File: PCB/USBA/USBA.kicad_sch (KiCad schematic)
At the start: 24 parts, among them J1 USB_A, J2 Shelly, J3 USB-PROG, U2 ESP32-S3-MINI-1, U5 MD8942, U7 SHT40

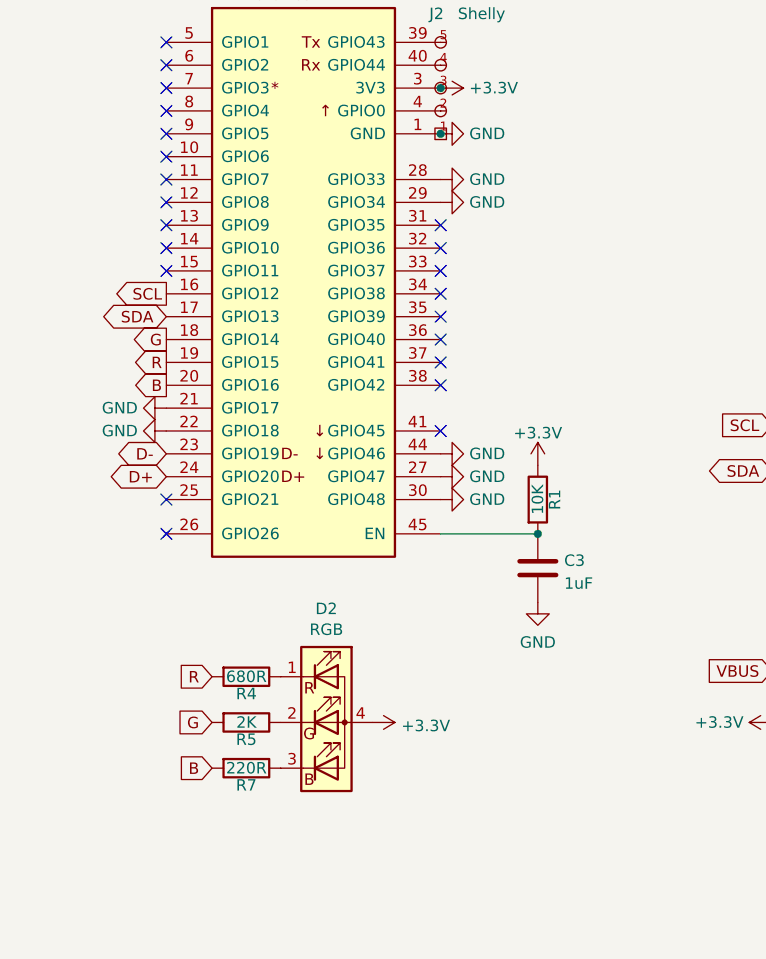
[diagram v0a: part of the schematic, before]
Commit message: Changed to WS2812
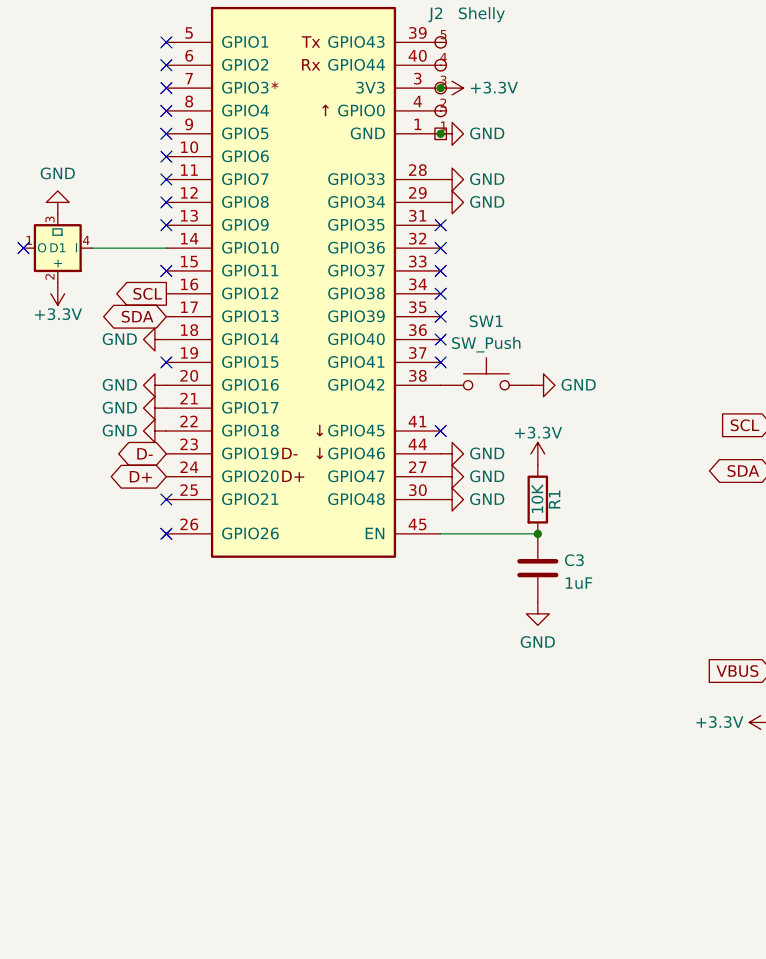
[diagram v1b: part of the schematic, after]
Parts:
- removed D2: RGB, RevK:LED-RGB-1.6x1.6, symbol Device:LED_RGBA
- removed R4: 680R, RevK:R_0402, symbol Device:R
- removed R5: 2K, RevK:R_0402, symbol Device:R
- removed R7: 220R, RevK:R_0402, symbol Device:R
- added D1: XL-1010RGBC-WS2812B, RevK:SMD1010, symbol RevK:WS2812B-1mm
- added SW1: SW_Push, RevK:TS-1092S-B3D2-G, symbol Switch:SW_Push
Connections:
- net B is gone; now on net GND: U2.20 (GPIO16)
- net G is gone; now on net GND: U2.18 (GPIO14)
- net +3.3V: now also D1.2 (+)
- net GND: now also D1.3 (⏚), SW1.2
- net at U2.14 (GPIO10): now also D1.4 (I)
- net at U2.38 (GPIO42): now also SW1.1
- net R: no longer names the net of U2.19 (GPIO15)

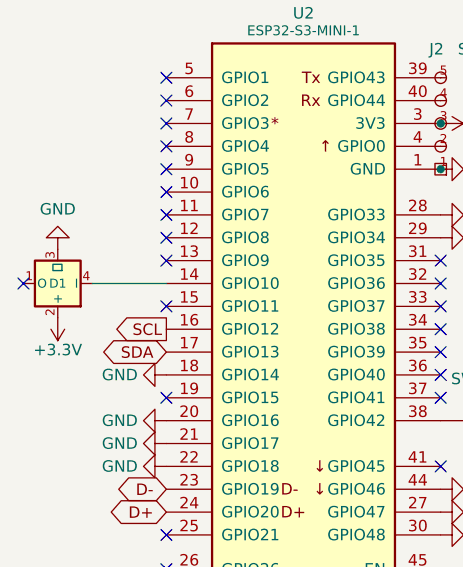
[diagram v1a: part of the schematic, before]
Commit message: Slight angle fixed
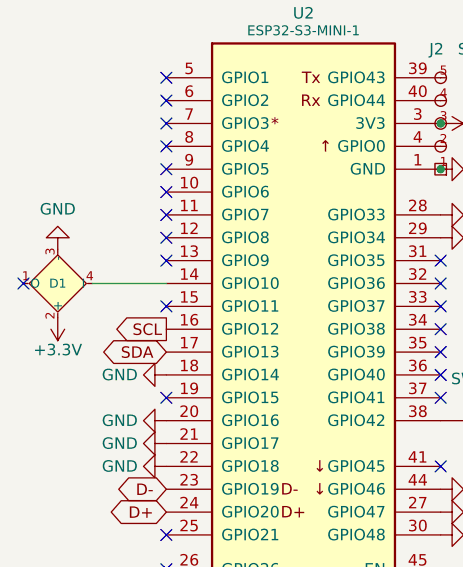
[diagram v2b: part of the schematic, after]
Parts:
- V1, V2: footprint RevK:VCUT70 -> RevK:VCUT70N
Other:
- moved on the sheet: D1
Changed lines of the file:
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@@
     )
   )
-  (symbol (lib_id "RevK:WS2812B-1mm") (at 81.915 75.565 180) (unit 1)
-    (in_bom yes) (on_board yes) (dnp no) (fields_autoplaced)
+  (symbol (lib_id "RevK:WS2812B-1mm") (at 81.915 75.565 0) (mirror y) (unit 1)
+    (in_bom yes) (on_board yes) (dnp no)
     (property "Reference" "D1" (at 81.915 75.565 0) (do_not_autoplace)
       (effects (font (size 1 1)))
     )
-    (property "Value" "XL-1010RGBC-WS2812B" (at 80.645 69.85 0)
+    (property "Value" "XL-1010RGBC-WS2812B" (at 80.645 81.28 0)
       (effects (font (size 1 1)) (justify left top) hide)
     )
-    (property "Footprint" "RevK:SMD1010" (at 80.645 67.945 0)
+    (property "Footprint" "RevK:SMD1010" (at 80.645 83.185 0)
       (effects (font (size 1 1)) (justify left top) hide)
     )
-    (property "Datasheet" "https://datasheet.lcsc.com/lcsc/2301111010_XINGLIGHT-XL-1010RGBC-WS2812B_C5349953.pdf" (at 80.645 66.04 0)
+    (property "Datasheet" "https://datasheet.lcsc.com/lcsc/2301111010_XINGLIGHT-XL-1010RGBC-WS2812B_C5349953.pdf" (at 80.645 85.09 0)
       (effects (font (size 1 1)) (justify left top) hide)
     )
-    (property "LCSC Part #" "C5349953" (at 80.645 64.135 0)
+    (property "LCSC Part #" "C5349953" (at 80.645 86.995 0)
       (effects (font (size 1 1)) (justify left top) hide)
     )
@@
       (effects (font (size 1.27 1.27)) hide)
     )
-    (property "Footprint" "RevK:VCUT70" (at 250.19 177.165 0)
+    (property "Footprint" "RevK:VCUT70N" (at 250.19 177.165 0)
       (effects (font (size 1.27 1.27)) hide)
     )
@@
       (effects (font (size 1.27 1.27)) hide)
     )
-    (property "Footprint" "RevK:VCUT70" (at 250.19 170.815 0)
+    (property "Footprint" "RevK:VCUT70N" (at 250.19 170.815 0)
       (effects (font (size 1.27 1.27)) hide)
     )

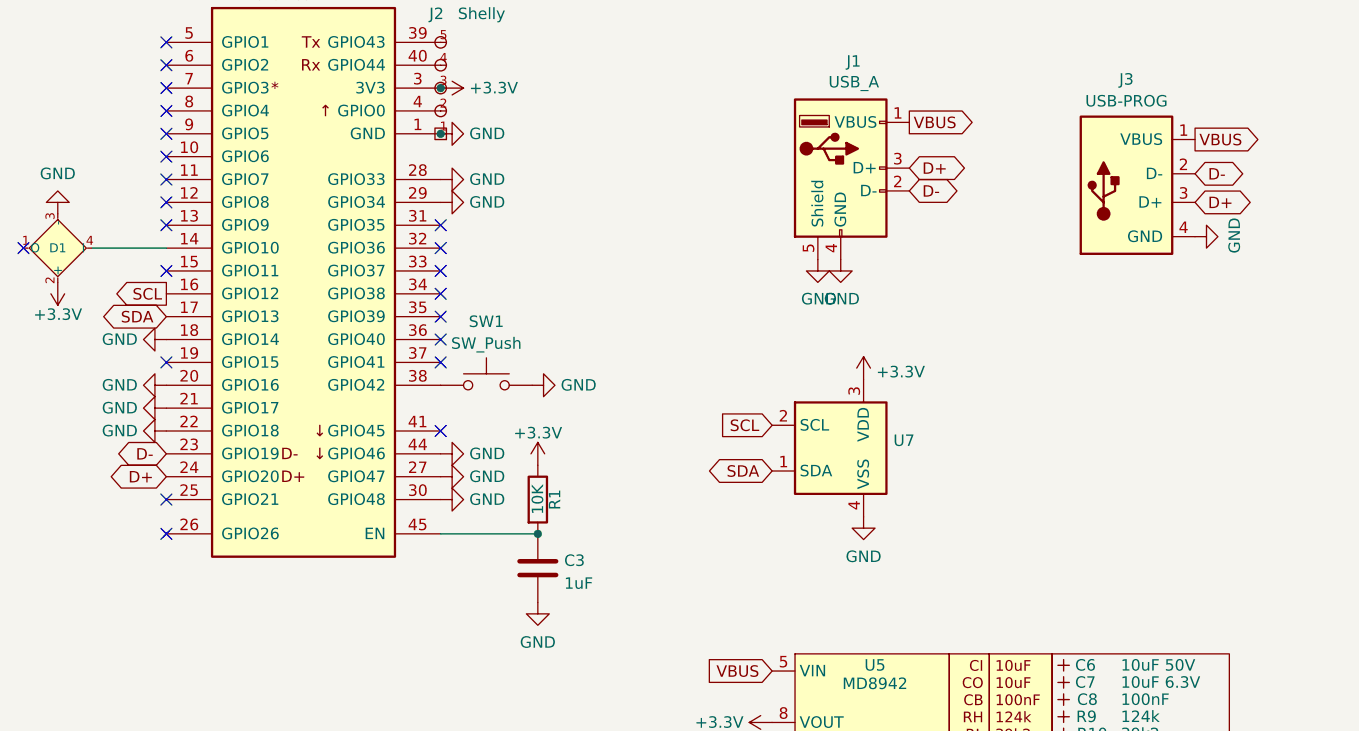
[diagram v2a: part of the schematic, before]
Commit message: Changed to light sensor
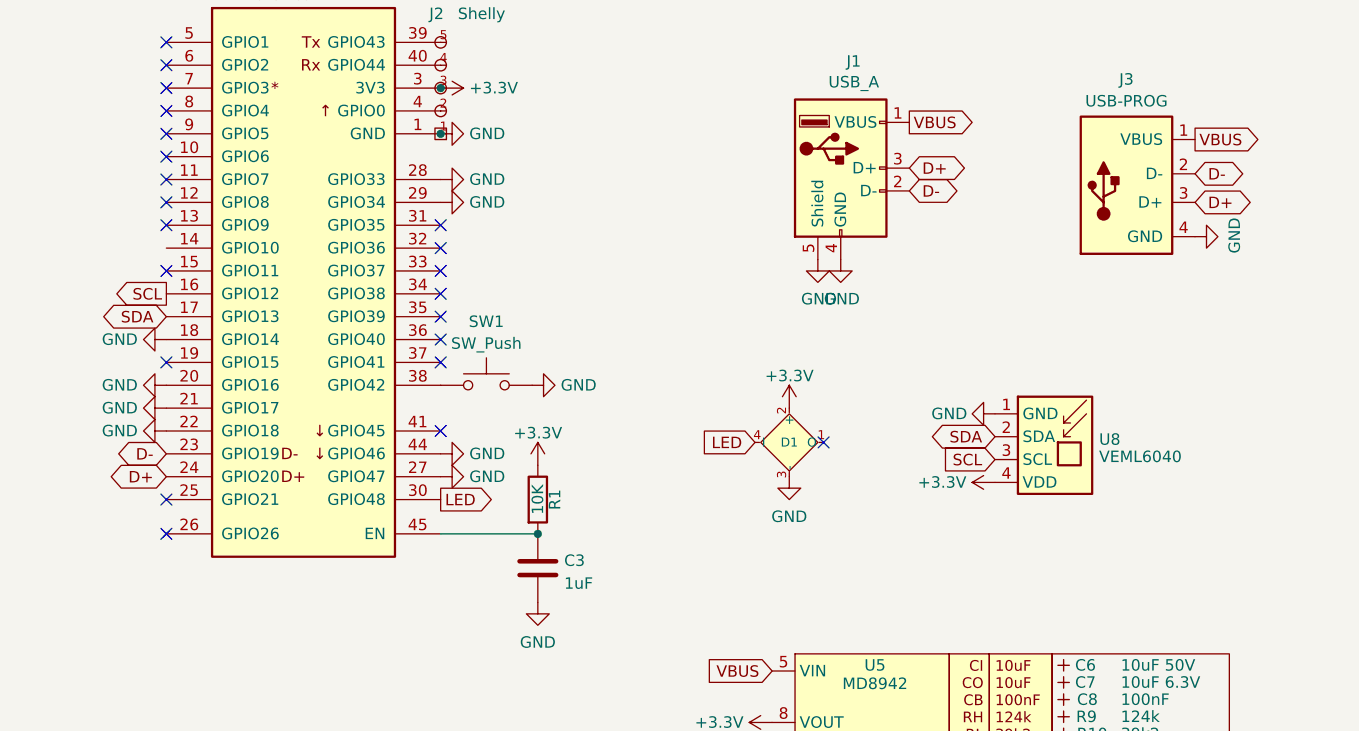
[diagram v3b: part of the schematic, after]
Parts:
- removed U7: SHT40, RevK:Sensirion_DFN-4_1.5x1.5mm_P0.5mm_SHT4x, symbol RevK:SHT40
- added U8: VEML6040, RevK:VEML6040, symbol RevK:VEML6040
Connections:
- net +3.3V: now also U8.4 (VDD)
- net GND: now also U8.1 (GND); no longer U2.30 (GPIO48)
- net SCL: now also U8.3 (SCL)
- net SDA: now also U8.2 (SDA)
- net at U2.14 (GPIO10): no longer D1.4 (I)
- new net LED: D1.4 (I), U2.30 (GPIO48)
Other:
- moved on the sheet: D1

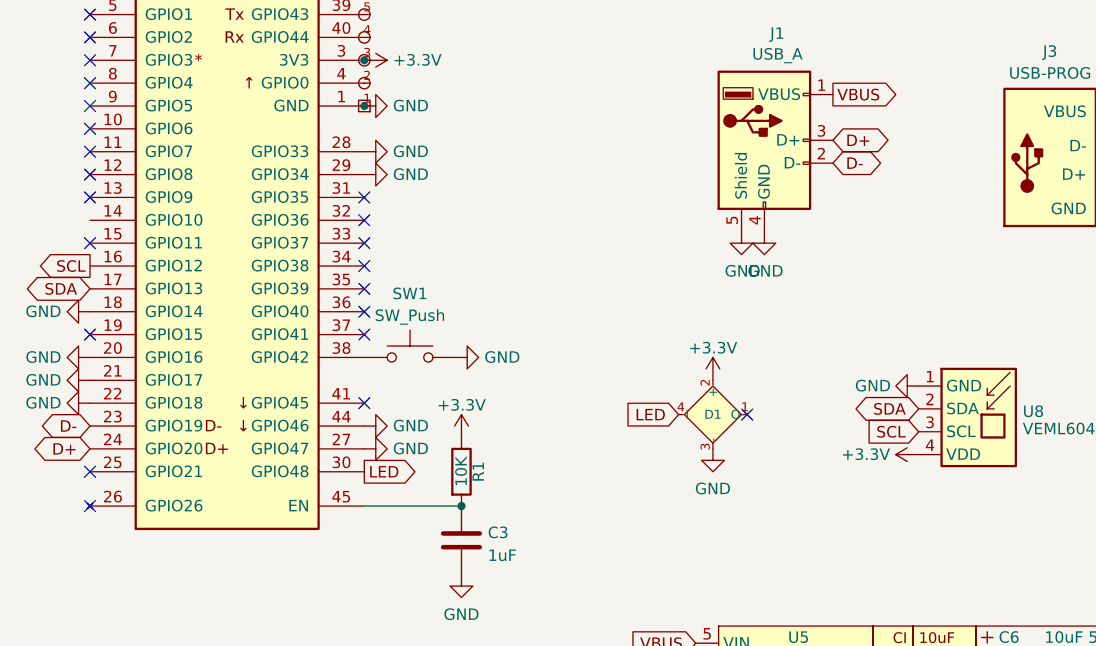
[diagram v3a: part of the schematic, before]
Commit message: Added 3 pads for LED
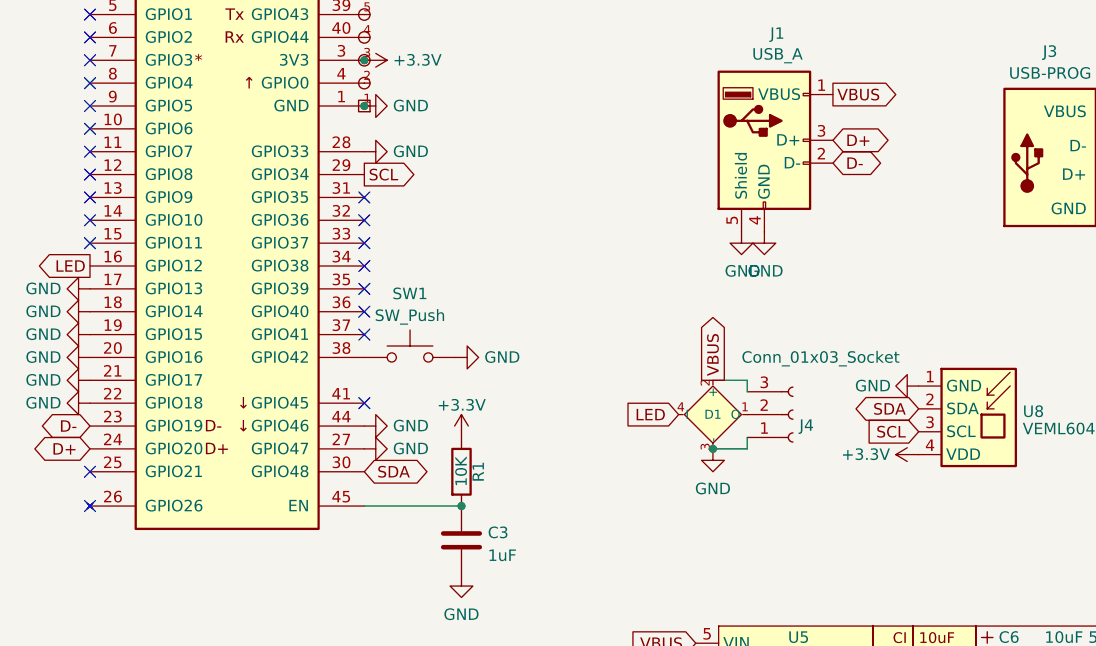
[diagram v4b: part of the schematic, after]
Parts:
- added J4: Conn_01x03_Socket, RevK:PinHeader_1x03_P2.54mm, symbol Connector:Conn_01x03_Socket
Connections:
- net +3.3V: no longer D1.2 (+)
- net GND: now also U2.17 (GPIO13), U2.19 (GPIO15), J4.1 (Pin_1); no longer U2.29 (GPIO34)
- net LED: now also U2.16 (GPIO12); no longer U2.30 (GPIO48)
- net SCL: now also U2.29 (GPIO34); no longer U2.16 (GPIO12)
- net SDA: now also U2.30 (GPIO48); no longer U2.17 (GPIO13)
- net VBUS: now also D1.2 (+), J4.3 (Pin_3)
- net at D1.1 (O): now also J4.2 (Pin_2)
- no-connect marks 23 -> 22
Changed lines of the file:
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@@
   (junction (at 124.46 62.865) (diameter 0) (color 0 0 0 0)
   )
+  (junction (at 163.195 100.965) (diameter 0) (color 0 0 0 0)
+  )
   (junction (at 135.255 107.315) (diameter 0) (color 0 0 0 0)
   )
   (no_connect (at 93.98 73.025))
-  (no_connect (at 167.005 97.155))
-  (no_connect (at 93.98 88.265))
   (no_connect (at 93.98 52.705))
   (no_connect (at 93.98 65.405))
@@
   (no_connect (at 124.46 78.105))
   (no_connect (at 124.46 80.645))
+  (no_connect (at 93.98 75.565))
   (no_connect (at 93.98 67.945))
   (no_connect (at 93.98 60.325))
@@
     (stroke (width 0) (type default))
   )
+  (wire (pts (xy 163.195 93.345) (xy 167.005 93.345))
+    (stroke (width 0) (type default))
+  )
+  (wire (pts (xy 167.005 93.345) (xy 167.005 94.615))
+    (stroke (width 0) (type default))
+  )
+  (wire (pts (xy 163.195 100.965) (xy 167.005 100.965))
+    (stroke (width 0) (type default))
+  )
+  (wire (pts (xy 167.005 100.965) (xy 167.005 99.695))
+    (stroke (width 0) (type default))
+  )
   (global_label "D+" (shape bidirectional) (at 176.53 66.675 0) (fields_autoplaced)
     (effects (font (size 1.27 1.27)) (justify left))
@@
     )
   )
+  (global_label "VBUS" (shape output) (at 163.195 93.345 90) (fields_autoplaced)
+    (effects (font (size 1.27 1.27)) (justify left))
+    (property "Intersheetrefs" "${INTERSHEET_REFS}" (at 163.195 86.1154 90)
+      (effects (font (size 1.27 1.27)) (justify left) hide)
+    )
+  )
   (global_label "D-" (shape bidirectional) (at 93.98 98.425 180) (fields_autoplaced)
     (effects (font (size 1.27 1.27)) (justify right))
@@
     )
   )
-  (global_label "SCL" (shape output) (at 93.98 80.645 180) (fields_autoplaced)
-    (effects (font (size 1.27 1.27)) (justify right))
-    (property "Intersheetrefs" "${INTERSHEET_REFS}" (at 88.2208 80.645 0)
-      (effects (font (size 1.27 1.27)) (justify right) hide)
+  (global_label "SCL" (shape output) (at 124.46 70.485 0) (fields_autoplaced)
+    (effects (font (size 1.27 1.27)) (justify left))
+    (property "Intersheetrefs" "${INTERSHEET_REFS}" (at 130.2986 70.485 0)
+      (effects (font (size 1.27 1.27)) (justify left) hide)
     )
   )
@@
     )
   )
-  (global_label "LED" (shape output) (at 124.46 103.505 0) (fields_autoplaced)
+  (global_label "LED" (shape output) (at 93.98 80.645 180) (fields_autoplaced)
+    (effects (font (size 1.27 1.27)) (justify right))
+    (property "Intersheetrefs" "${INTERSHEET_REFS}" (at 88.2019 80.645 0)
+      (effects (font (size 1.27 1.27)) (justify right) hide)
+    )
+  )
+  (global_label "SDA" (shape bidirectional) (at 124.46 103.505 0) (fields_autoplaced)
     (effects (font (size 1.27 1.27)) (justify left))
-    (property "Intersheetrefs" "${INTERSHEET_REFS}" (at 130.2381 103.505 0)
+    (property "Intersheetrefs" "${INTERSHEET_REFS}" (at 131.3116 103.505 0)
       (effects (font (size 1.27 1.27)) (justify left) hide)
-    )
-  )
-  (global_label "SDA" (shape bidirectional) (at 93.98 83.185 180) (fields_autoplaced)
-    (effects (font (size 1.27 1.27)) (justify right))
-    (property "Intersheetrefs" "${INTERSHEET_REFS}" (at 88.0877 83.1056 0)
-      (effects (font (size 1.27 1.27)) (justify right) hide)
     )
   )
@@
     )
   )
+  (symbol (lib_id "power:GND") (at 93.98 83.185 270) (unit 1)
+    (in_bom yes) (on_board yes) (dnp no) (fields_autoplaced)
+    (property "Reference" "#PWR04" (at 87.63 83.185 0)
+      (effects (font (size 1.27 1.27)) hide)
+    )
+    (property "Value" "GND" (at 90.8051 83.185 90)
+      (effects (font (size 1.27 1.27)) (justify right))
+    )
+    (property "Footprint" "" (at 93.98 83.185 0)
+      (effects (font (size 1.27 1.27)) hide)
+    )
+    (property "Datasheet" "" (at 93.98 83.185 0)
+      (effects (font (size 1.27 1.27)) hide)
+    )
+    (pin "1")
+    (instances
+      (project "USBA"
+        (path "/2d210a96-f81f-42a9-8bf4-1b43c11086f3"
+          (reference "#PWR04") (unit 1)
+        )
+      )
+    )
+  )
   (symbol (lib_id "power:+3.3V") (at 135.255 99.695 0) (unit 1)
     (in_bom yes) (on_board yes) (dnp no) (fields_autoplaced)
@@
     )
   )
+  (symbol (lib_id "power:GND") (at 93.98 88.265 270) (unit 1)
+    (in_bom yes) (on_board yes) (dnp no) (fields_autoplaced)
+    (property "Reference" "#PWR020" (at 87.63 88.265 0)
+      (effects (font (size 1.27 1.27)) hide)
+    )
+    (property "Value" "GND" (at 90.8051 88.265 90)
+      (effects (font (size 1.27 1.27)) (justify right))
+    )
+    (property "Footprint" "" (at 93.98 88.265 0)
+      (effects (font (size 1.27 1.27)) hide)
+    )
+    (property "Datasheet" "" (at 93.98 88.265 0)
+      (effects (font (size 1.27 1.27)) hide)
+    )
+    (pin "1")
+    (instances
+      (project "USBA"
+        (path "/2d210a96-f81f-42a9-8bf4-1b43c11086f3"
+          (reference "#PWR020") (unit 1)
+        )
+      )
+    )
+  )
   (symbol (lib_id "RevK:VEML6040") (at 193.04 97.155 0) (unit 1)
     (in_bom yes) (on_board yes) (dnp no)
@@
         (path "/babeabf2-f3b0-4ed5-8d9e-0215947e6cf3"
           (reference "#PWR024") (unit 1)
-        )
-      )
-    )
-  )
-  (symbol (lib_id "power:+3.3V") (at 163.195 93.345 0) (unit 1)
-    (in_bom yes) (on_board yes) (dnp no) (fields_autoplaced)
-    (property "Reference" "#PWR04" (at 163.195 97.155 0)
-      (effects (font (size 1.27 1.27)) hide)
-    )
-    (property "Value" "+3.3V" (at 163.195 89.7692 0)
-      (effects (font (size 1.27 1.27)))
-    )
-    (property "Footprint" "" (at 163.195 93.345 0)
-      (effects (font (size 1.27 1.27)) hide)
-    )
-    (property "Datasheet" "" (at 163.195 93.345 0)
-      (effects (font (size 1.27 1.27)) hide)
-    )
-    (pin "1")
-    (instances
-      (project "USBA"
-        (path "/2d210a96-f81f-42a9-8bf4-1b43c11086f3"
-          (reference "#PWR04") (unit 1)
         )
       )
@@
     )
   )
+  (symbol (lib_id "Connector:Conn_01x03_Socket") (at 172.085 97.155 0) (mirror x) (unit 1)
+    (in_bom no) (on_board yes) (dnp no)
+    (property "Reference" "J4" (at 172.7962 98.3671 0)
+      (effects (font (size 1.27 1.27)) (justify left))
+    )
+    (property "Value" "Conn_01x03_Socket" (at 166.37 90.805 0)
+      (effects (font (size 1.27 1.27)) (justify left))
+    )
+    (property "Footprint" "RevK:PinHeader_1x03_P2.54mm" (at 172.085 97.155 0)
+      (effects (font (size 1.27 1.27)) hide)
+    )
+    (property "Datasheet" "~" (at 172.085 97.155 0)
+      (effects (font (size 1.27 1.27)) hide)
+    )
+    (pin "1")
+    (pin "2")
+    (pin "3")
+    (instances
+      (project "USBA"
+        (path "/2d210a96-f81f-42a9-8bf4-1b43c11086f3"
+          (reference "J4") (unit 1)
+        )
+      )
+    )
+  )
   (symbol (lib_id "power:GND") (at 172.72 137.795 0) (unit 1)
     (in_bom yes) (on_board yes) (dnp no)
@@
         )
       )
-    )
-  )
-  (symbol (lib_id "power:GND") (at 124.46 70.485 90) (unit 1)
-    (in_bom yes) (on_board yes) (dnp no) (fields_autoplaced)
-    (property "Reference" "#PWR016" (at 130.81 70.485 0)
-      (effects (font (size 1.27 1.27)) hide)
-    )
-    (property "Value" "GND" (at 127.635 70.485 90)
-      (effects (font (size 1.27 1.27)) (justify right))
-    )
-    (property "Footprint" "" (at 124.46 70.485 0)
-      (effects (font (size 1.27 1.27)) hide)
-    )
-    (property "Datasheet" "" (at 124.46 70.485 0)
-      (effects (font (size 1.27 1.27)) hide)
-    )
-    (pin "1")
-    (instances
-      (project "USBA"
-        (path "/2d210a96-f81f-42a9-8bf4-1b43c11086f3"
-          (reference "#PWR016") (unit 1)
-        )
-      )
